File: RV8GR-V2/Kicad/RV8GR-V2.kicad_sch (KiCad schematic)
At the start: 2 parts

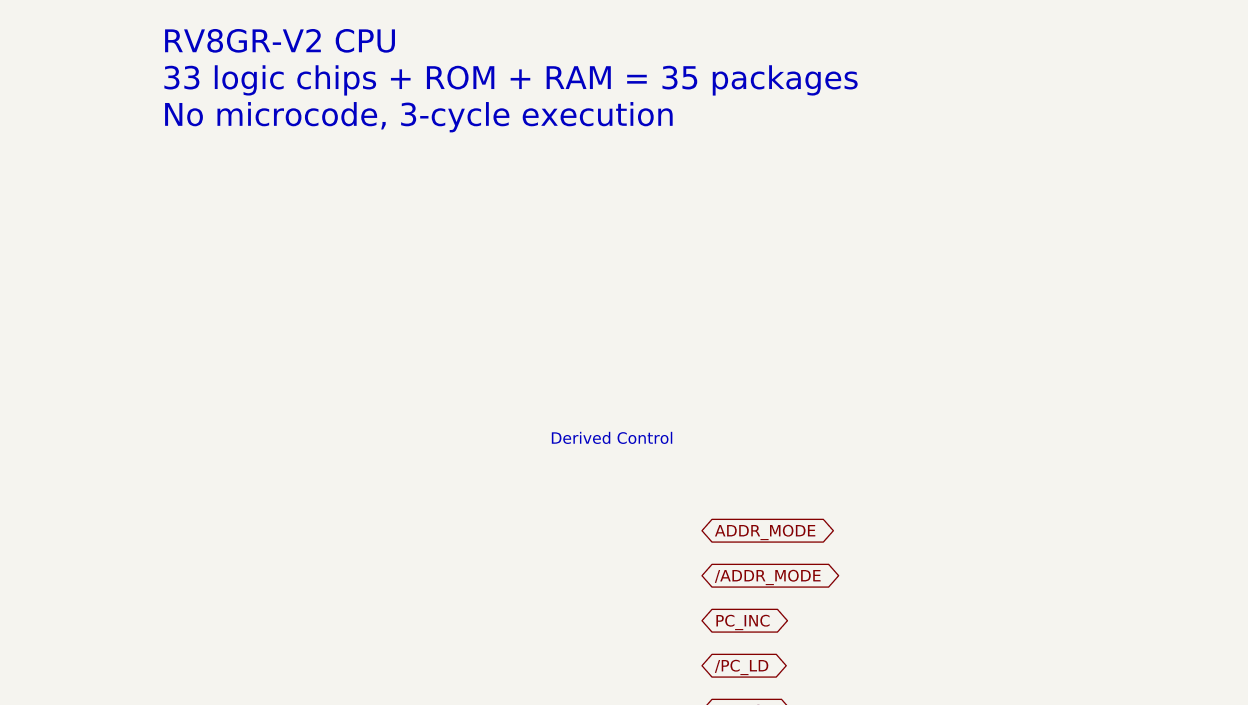
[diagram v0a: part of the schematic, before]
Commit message: Fix RV8GR-V2 chip-level docs and netlist
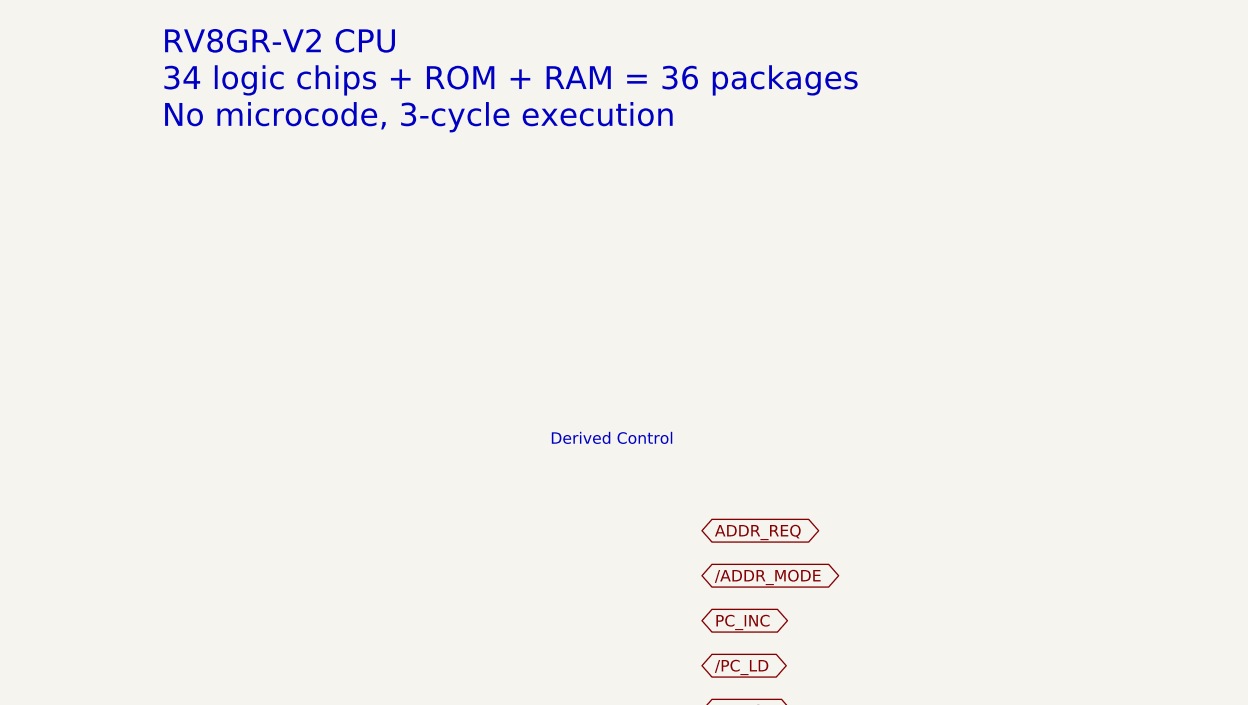
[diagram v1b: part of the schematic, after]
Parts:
- removed ?: (no value), symbol power:GND
- removed ?: (no value), symbol power:VCC
- added ?: (no value), symbol power:GND
- added ?: (no value), symbol power:VCC
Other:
- note added: "RV8GR-V2 CPU 34 logic chips + ROM + RAM = 36 packages No microcode, 3-cycle execution"
- note removed: "RV8GR-V2 CPU 33 logic chips + ROM + RAM = 35 packages No microcode, 3-cycle execution"
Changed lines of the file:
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@@
     (rev "v2.0")
     (company "RV8 Project")
-    (comment 1 "33 logic chips + ROM + RAM = 35 packages")
+    (comment 1 "34 logic chips + ROM + RAM = 36 packages")
   )
-  (text "RV8GR-V2 CPU\n33 logic chips + ROM + RAM = 35 packages\nNo microcode, 3-cycle execution"
+  (text "RV8GR-V2 CPU\n34 logic chips + ROM + RAM = 36 packages\nNo microcode, 3-cycle execution"
     (at 100 20 0)
     (effects (font (size 2.54 2.54)) (justify left))
@@
   )
   (text "Derived Control" (at 150 60 0) (effects (font (size 1.27 1.27))))
-  (global_label "ADDR_MODE" (shape bidirectional) (at 160 70 0)
+  (global_label "ADDR_REQ" (shape bidirectional) (at 160 70 0)
     (fields_autoplaced yes)
     (effects (font (size 1.27 1.27)) (justify left))
